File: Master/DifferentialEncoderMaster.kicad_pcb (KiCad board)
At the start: 2 copper layers, 53 x 131 mm, 41 parts, among them J1 RJ45_Shielded, J10 Conn_02x06_Top_Bottom, J11 Conn_02x06_Top_Bottom, J12 CAN_Header, J2 Conn_01x06, J3 Conn_01x20, J4 Conn_01x12, J5 RJ45_Shielded, J6 RJ45_Shielded, J7 RJ45_Shielded, J8 Jumper, J9 Jumper, U1 SN75C1167, U2 SN75C1167, U3 ST26C32ABTR, U4 ST26C32ABTR

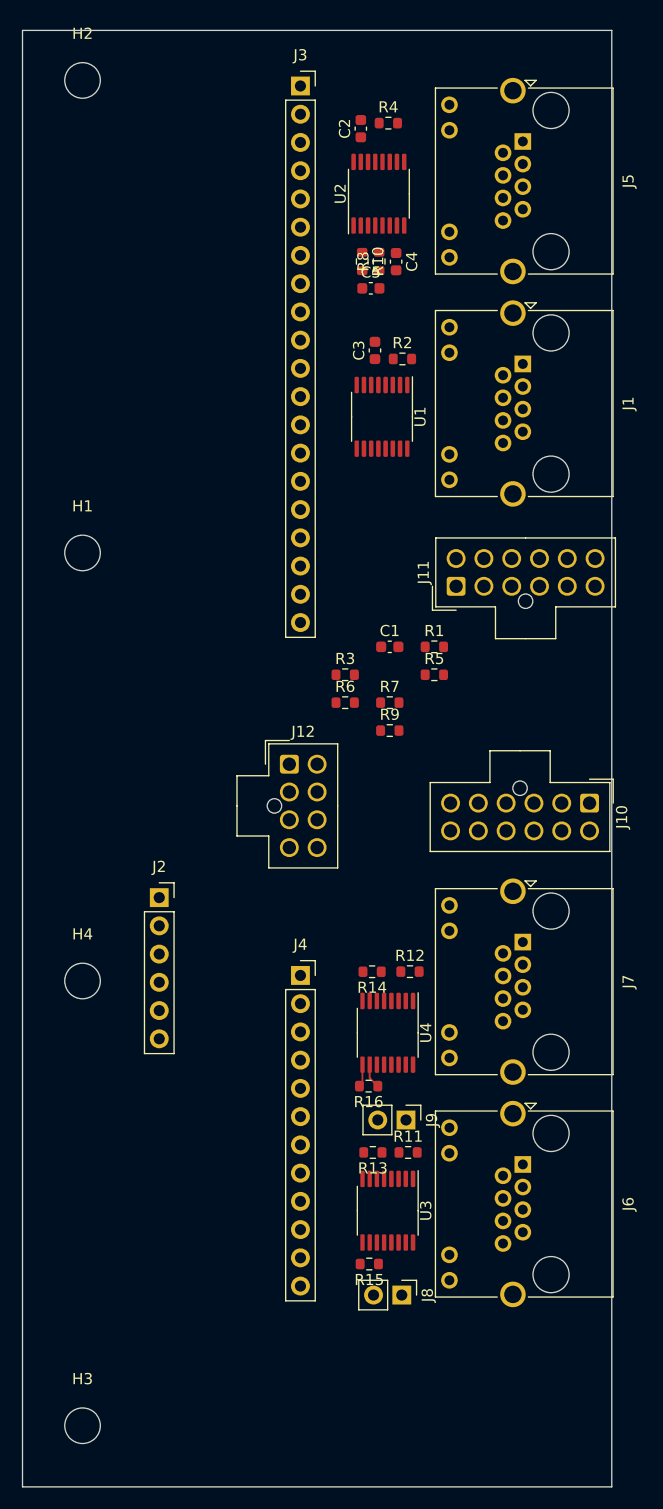
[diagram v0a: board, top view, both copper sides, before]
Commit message: Add digital isolators
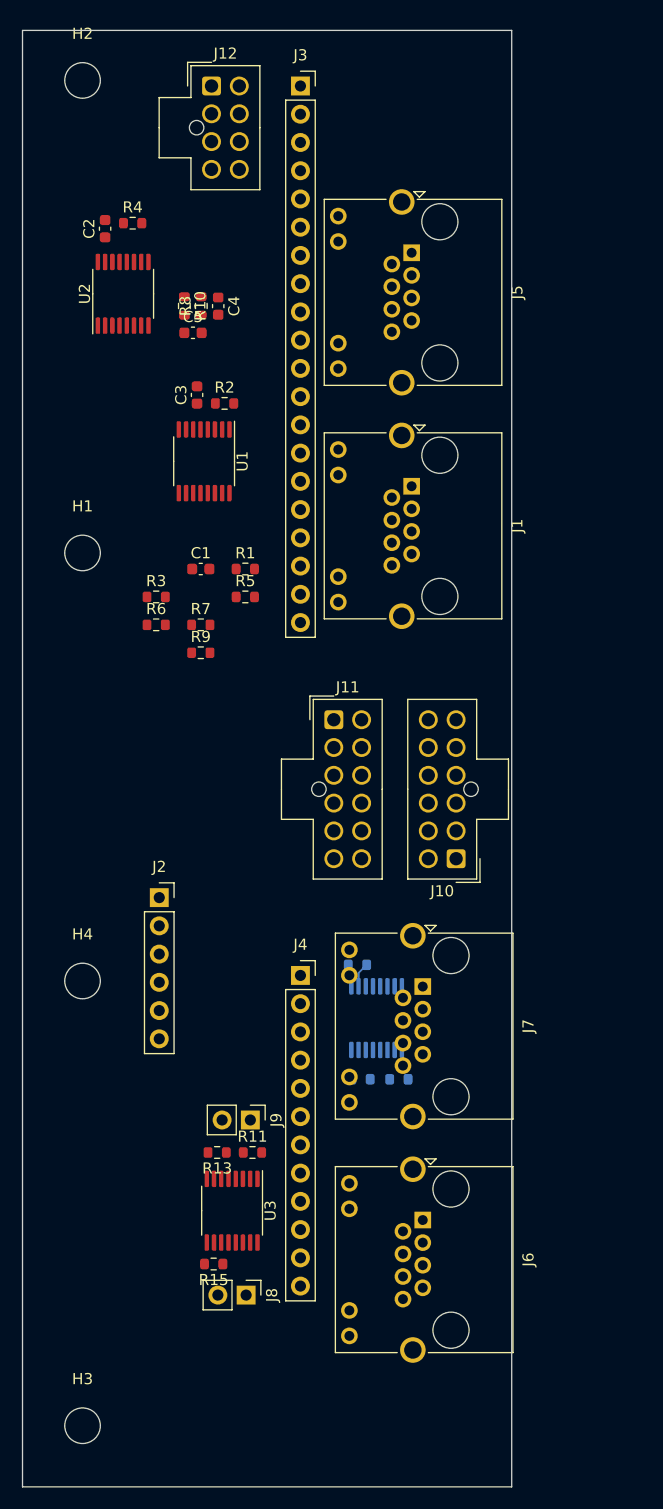
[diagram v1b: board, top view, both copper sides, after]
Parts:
- R12, R14, R16, U4: moved to B.Cu
- moved J12 61.4 mm to (117.0, 50.0)
- moved C2 24.7 mm to (107.4, 62.8)
- moved R4 24.7 mm to (109.9, 62.3)
- moved U2 24.7 mm to (109.1, 68.7)
- moved C1 18.4 mm to (116.0, 93.4)
- moved R7 18.4 mm to (116.0, 98.5)
- moved R9 18.4 mm to (116.0, 101.0)
- moved R1 18.4 mm to (120.0, 93.4)
- moved R3 18.4 mm to (112.0, 96.0)
- moved R5 18.4 mm to (120.0, 96.0)
- moved R6 18.4 mm to (112.0, 98.5)
- moved C3 16.5 mm to (115.7, 77.8)
- moved C4 16.5 mm to (117.6, 69.8)
- moved R10 16.5 mm to (114.6, 69.8)
- moved R2 16.5 mm to (118.2, 78.5)
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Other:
- board size 53 x 131 mm -> 44 x 131 mm

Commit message: Big updates to master
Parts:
- removed J6, J7: RJ45_Shielded, Connector_RJ:RJ45_Amphenol_RJHSE538X
- added C10: 100nF, Capacitor_SMD:C_0603_1608Metric, F.Cu at (142.6, 122.6)
- added C11: 100nF, Capacitor_SMD:C_0603_1608Metric, F.Cu at (142.0, 165.9)
- added C6: 100nF, Capacitor_SMD:C_0603_1608Metric, F.Cu at (136.9, 96.5)
- added C7: 100nF, Capacitor_SMD:C_0603_1608Metric, F.Cu at (116.5, 80.1)
- added C8: 100nF, Capacitor_SMD:C_0603_1608Metric, F.Cu at (129.3, 55.5)
- added C9: 100nF, Capacitor_SMD:C_0603_1608Metric, F.Cu at (114.8, 83.2)
- added FB1: 1kR, Inductor_SMD:L_0603_1608Metric, F.Cu at (114.8, 80.0)
- added FB2: 1kR, Inductor_SMD:L_0603_1608Metric, F.Cu at (116.5, 83.2)
- added J13: ISO_GPIO, Connector_Molex:Molex_Nano-Fit_105310-xx08_2x04_P2.50mm_Vertical, F.Cu at (107.2, 71.8)
- added R17: 3.3k, Resistor_SMD:R_0603_1608Metric, F.Cu at (142.0, 168.5)
- added R18: 3.3k, Resistor_SMD:R_0603_1608Metric, F.Cu at (142.6, 125.2)
- added R19: 0R, Resistor_SMD:R_0603_1608Metric, F.Cu at (135.3, 49.4)
- added R20: 0R, Resistor_SMD:R_0603_1608Metric, F.Cu at (134.9, 104.0)
- added U6: ISO7761DBQ, Package_SO:SSOP-16_3.9x4.9mm_P0.635mm, F.Cu at (111.0, 81.6)
- J1, J5: value RJ45_Shielded -> RJ45_Shielded_x2; footprint Connector_RJ:RJ45_Amphenol_RJHSE538X -> Wetmelon:RJ45_RJSSE5380-02
- J10: value Conn_02x06_Top_Bottom -> Encoder_0
- J11: value Conn_02x06_Top_Bottom -> Encoder_1
- R12, R14, R16, U4: moved to F.Cu
- moved J5 92.7 mm to (128.9, 157.5), turned to 90 degrees
- moved R5 50.9 mm to (142.8, 50.4), turned to 270 degrees
- moved J10 49.9 mm to (105.8, 156.8), turned to 90 degrees
- moved C1 49.8 mm to (141.2, 50.4), turned to 90 degrees
- moved R7 49.4 mm to (129.5, 50.9)
- moved C2 48.6 mm to (140.5, 98.4), turned to 0 degrees
- moved R3 46.5 mm to (129.5, 52.9)
- moved R8 42.0 mm to (140.5, 104.0), turned to 180 degrees
- moved J11 40.9 mm to (118.2, 146.8), turned to 270 degrees
- moved R4 40.9 mm to (129.7, 98.1), turned to 90 degrees
- moved U2 40.6 mm to (134.8, 100.0), turned to 0 degrees
- moved C4 39.7 mm to (140.5, 102.3), turned to 0 degrees
- moved U1 36.0 mm to (135.4, 53.2), turned to 180 degrees
- moved R16 35.5 mm to (137.2, 163.8), turned to 0 degrees
- moved U4 34.6 mm to (136.4, 168.1), turned to 0 degrees
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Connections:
- J1 pad 10: (no net) -> /CSn_2-
- J1 pad 11: (no net) -> /CLK_2+
- J1 pad 12: (no net) -> /MISO_2-
- J1 pad 9: (no net) -> /CSn_2+
- J10 pad 12: /AGND -> (no net)
- J10 pad 6: /GPIO5 -> (no net)
- J11 pad 12: /AGND -> (no net)
- J11 pad 6: /GPIO6 -> (no net)
- J2 pad 3: /SWC -> (no net)
- J2 pad 5: /SWD -> (no net)
- J2 pad 6: /~RST -> (no net)
- J3 pad 10: /MOSI -> (no net)
- J3 pad 6: /AVCC -> (no net)
- J3 pad 7: /AGND -> (no net)
- J5 pad 1: /CSn_2+ -> /ENC0_A+
- J5 pad 10: (no net) -> /ENC1_A-
- J5 pad 11: (no net) -> /ENC1_B+
- J5 pad 12: (no net) -> /ENC1_Z-
- J5 pad 2: /CSn_2- -> /ENC0_A-
- J5 pad 3: /CLK_2+ -> /ENC0_B+
- J5 pad 4: /MISO_2- -> /ENC0_Z-
- J5 pad 5: /MISO_2+ -> /ENC0_Z+
- J5 pad 6: /CLK_2- -> /ENC0_B-
- J5 pad 9: (no net) -> /ENC1_A+
- R7 pad 1: /GPIO7 -> /GPIO5
- R8 pad 1: /GPIO8 -> /GPIO6
- U1 pad 4: /CSn_1 -> Net-(R19-Pad2)
- U1 pad 5: Net-(U1-Pad5) -> (no net)
- U1 pad 6: Net-(U1-Pad6) -> (no net)
- U1 pad 7: Net-(U1-Pad7) -> (no net)
- U2 pad 4: /CSn_2 -> Net-(R20-Pad2)
- U2 pad 5: Net-(U2-Pad5) -> (no net)
- U2 pad 6: Net-(U2-Pad6) -> (no net)
- U2 pad 7: Net-(U2-Pad7) -> (no net)
- U3 pad 12: Net-(J8-Pad1) -> Net-(J9-Pad1)
- U3 pad 13: Net-(U3-Pad13) -> (no net)
- U3 pad 14: Net-(U3-Pad14) -> (no net)
- U3 pad 15: Net-(U3-Pad15) -> (no net)
- U3 pad 4: +5V -> GNDD
- U4 pad 12: Net-(J9-Pad1) -> Net-(J8-Pad1)
- U4 pad 13: Net-(U4-Pad13) -> (no net)
- U4 pad 14: Net-(U4-Pad14) -> (no net)
- U4 pad 15: Net-(U4-Pad15) -> (no net)
- U4 pad 4: +5V -> GNDD
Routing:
- net /CSn_2+: track 0.00 -> 32.5 mm, vias 0 -> 2
- net /CSn_2-: track 0.00 -> 30.7 mm, vias 0 -> 2
- net GNDD: track 0.00 -> 30.7 mm, vias 0 -> 10
- net /CLK_2-: track 0.00 -> 25.0 mm, vias 0 -> 2
- net /CLK_2+: track 0.00 -> 25.0 mm, vias 0 -> 2
- net +5V: track 0.00 -> 24.6 mm, vias 0 -> 7
- net /M1_Z: track 0.00 -> 23.5 mm
- net VDD1: track 0.00 -> 23.5 mm, vias 0 -> 1
- net /MISO_2-: track 0.00 -> 23.5 mm, vias 0 -> 2
- net /M1_B: track 0.00 -> 22.6 mm
- net /GPIO1: track 0.00 -> 22.1 mm
- net /MISO_2+: track 0.00 -> 22.1 mm, vias 0 -> 2
- net /M1_A: track 0.00 -> 21.4 mm
- net /M0_Z: track 0.00 -> 20.6 mm
- net /M0_A: track 0.00 -> 20.4 mm
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- added copper zone on In2.Cu, net +5V
- added copper zone on In1.Cu, net GNDD
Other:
- board size 44 x 131 mm -> 46.5 x 131 mm
- copper layers 2 -> 4
- net class Default: clearance 0.1651 -> 0.2032; trace_width 0.1651 -> 0.2032
- rule trace_clearance: 0.1651 -> 0.2032

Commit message: Finish rev 1 layout
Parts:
- moved J8 54.3 mm to (135.5, 118.9), turned to 90 degrees
- moved J9 51.0 mm to (136.0, 170.7), turned to 90 degrees
- moved C10 46.8 mm to (131.6, 168.1), turned to 180 degrees
- moved R14 46.2 mm to (141.9, 122.8), turned to 90 degrees
- moved R11 45.8 mm to (142.4, 167.6), turned to 270 degrees
- moved R17 45.0 mm to (131.4, 124.7), turned to 180 degrees
- moved U4 44.1 mm to (137.0, 124.1), turned to 180 degrees
- moved R18 42.7 mm to (131.6, 166.5), turned to 180 degrees
- moved R16 41.8 mm to (132.1, 122.3), turned to 90 degrees
- moved U3 40.9 mm to (137.2, 165.8), turned to 180 degrees
- moved C11 40.9 mm to (131.4, 126.4), turned to 180 degrees
- moved R13 39.7 mm to (142.4, 164.5), turned to 90 degrees
- moved R12 38.7 mm to (141.9, 126.0), turned to 270 degrees
- moved R15 37.8 mm to (132.1, 163.8)
- moved C3 14.9 mm to (141.7, 57.8), turned to 0 degrees
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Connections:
- J13 pad 1: VDD1 -> /ISO_STEP_2
- J13 pad 2: GND1 -> /ISO_DIR_2
- J13 pad 3: /ISO_DIR_1 -> /ISO_UART_RX
- J13 pad 4: /ISO_STEP_1 -> /ISO_UART_TX
- J13 pad 5: /ISO_UART_TX -> /ISO_STEP_1
- J13 pad 6: /ISO_UART_RX -> /ISO_DIR_1
- J13 pad 7: /ISO_DIR_2 -> GND1
- J13 pad 8: /ISO_STEP_2 -> VDD1
- J2 pad 2: /+3.3V -> (no net)
- J3 pad 1: /+3.3V -> (no net)
- J4 pad 1: /+3.3V -> (no net)
- J4 pad 7: /+3.3V -> (no net)
- J5 pad 1: /ENC0_A+ -> /ENC1_A+
- J5 pad 10: /ENC1_A- -> /ENC0_A-
- J5 pad 11: /ENC1_B+ -> /ENC0_B+
- J5 pad 12: /ENC1_Z- -> /ENC0_Z-
- J5 pad 13: /ENC1_Z+ -> /ENC0_Z+
- J5 pad 14: /ENC1_B- -> /ENC0_B-
- J5 pad 2: /ENC0_A- -> /ENC1_A-
- J5 pad 3: /ENC0_B+ -> /ENC1_B+
- J5 pad 4: /ENC0_Z- -> /ENC1_Z-
- J5 pad 5: /ENC0_Z+ -> /ENC1_Z+
- J5 pad 6: /ENC0_B- -> /ENC1_B-
- J5 pad 9: /ENC1_A+ -> /ENC0_A+
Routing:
- net /SCK: track 0.00 -> 72.7 mm, vias 0 -> 6
- net /MISO_2: track 0.00 -> 44.5 mm, vias 0 -> 2
- net /ENC0_A+: track 0.00 -> 43.2 mm, vias 0 -> 2
- net /GPIO5: track 0.00 -> 42.8 mm, vias 0 -> 3
- net /ENC0_A-: track 0.00 -> 41.2 mm, vias 0 -> 2
- net /ENC1_B-: track 0.00 -> 35.3 mm
- net /ENC1_B+: track 0.00 -> 33.8 mm
- net /M0_A: track 20.4 -> 53.1 mm, vias 0 -> 1
- net /ENC0_B+: track 0.00 -> 32.4 mm, vias 0 -> 1
- net /M1_B: track 22.6 -> 54.3 mm, vias 0 -> 3
- net /GPIO6: track 0.00 -> 31.2 mm, vias 0 -> 1
- net /ENC1_A-: track 0.00 -> 31.1 mm, vias 0 -> 2
- net /ENC0_B-: track 0.00 -> 31.0 mm, vias 0 -> 1
- net /M0_Z: track 20.6 -> 51.4 mm, vias 0 -> 1
- net /ENC1_A+: track 0.00 -> 30.6 mm, vias 0 -> 2
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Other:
- board text added: "+5V"
- board text added: "CAN"
- board text added: "CANH"
- board text added: "CANL"
- board text added: "DIR1"
- board text added: "DIR2"
- board text added: "GND"
- board text added: "GND1"
- board text added: "GND1 / VDD1 Isolated"
- board text added: "GPIO"
- board text added: "STEP1"
- board text added: "STEP2"
- board text added: "U_RX"
- board text added: "U_TX"
- board text added: "VDD1"

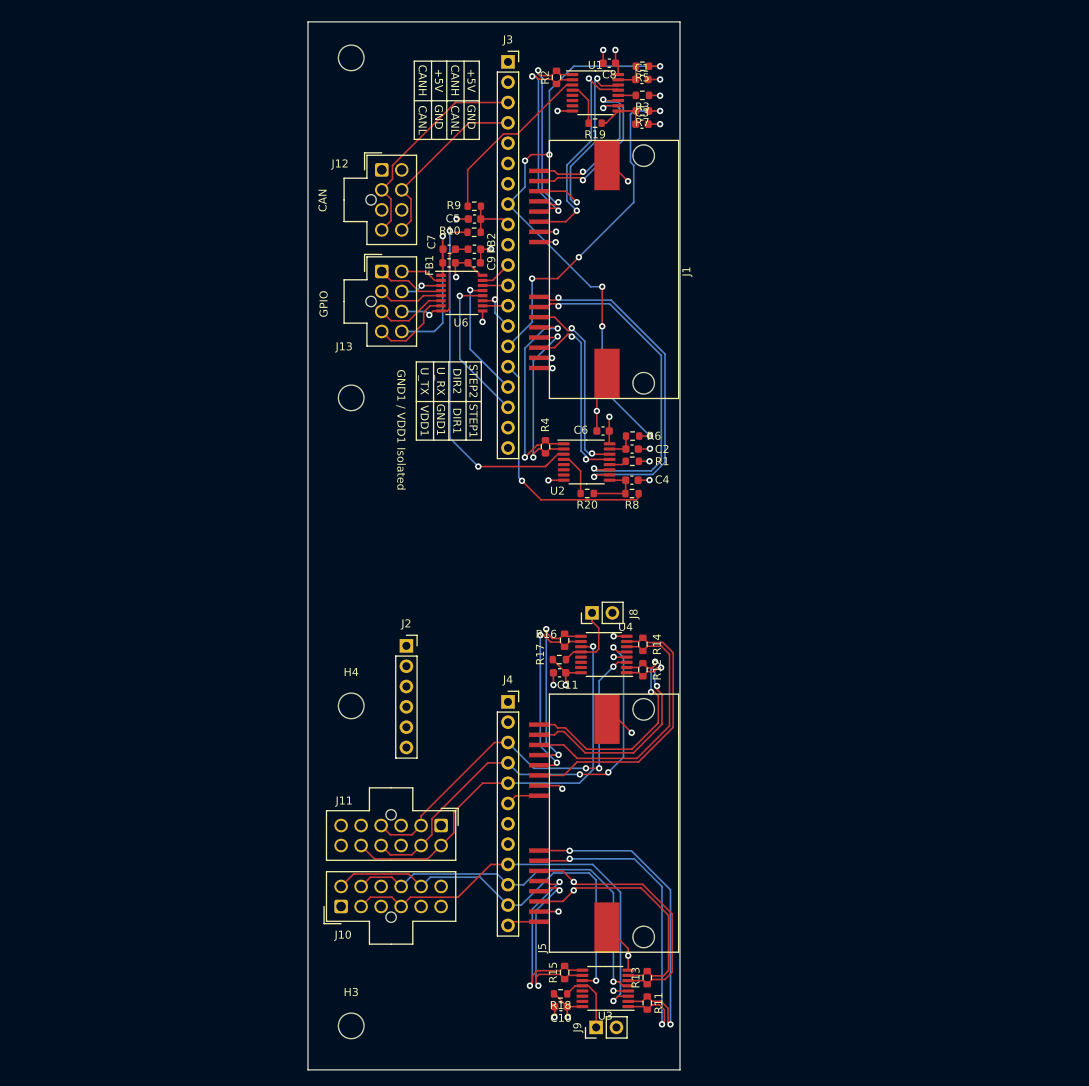
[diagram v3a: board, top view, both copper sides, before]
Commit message: Rotate board and recreate planes
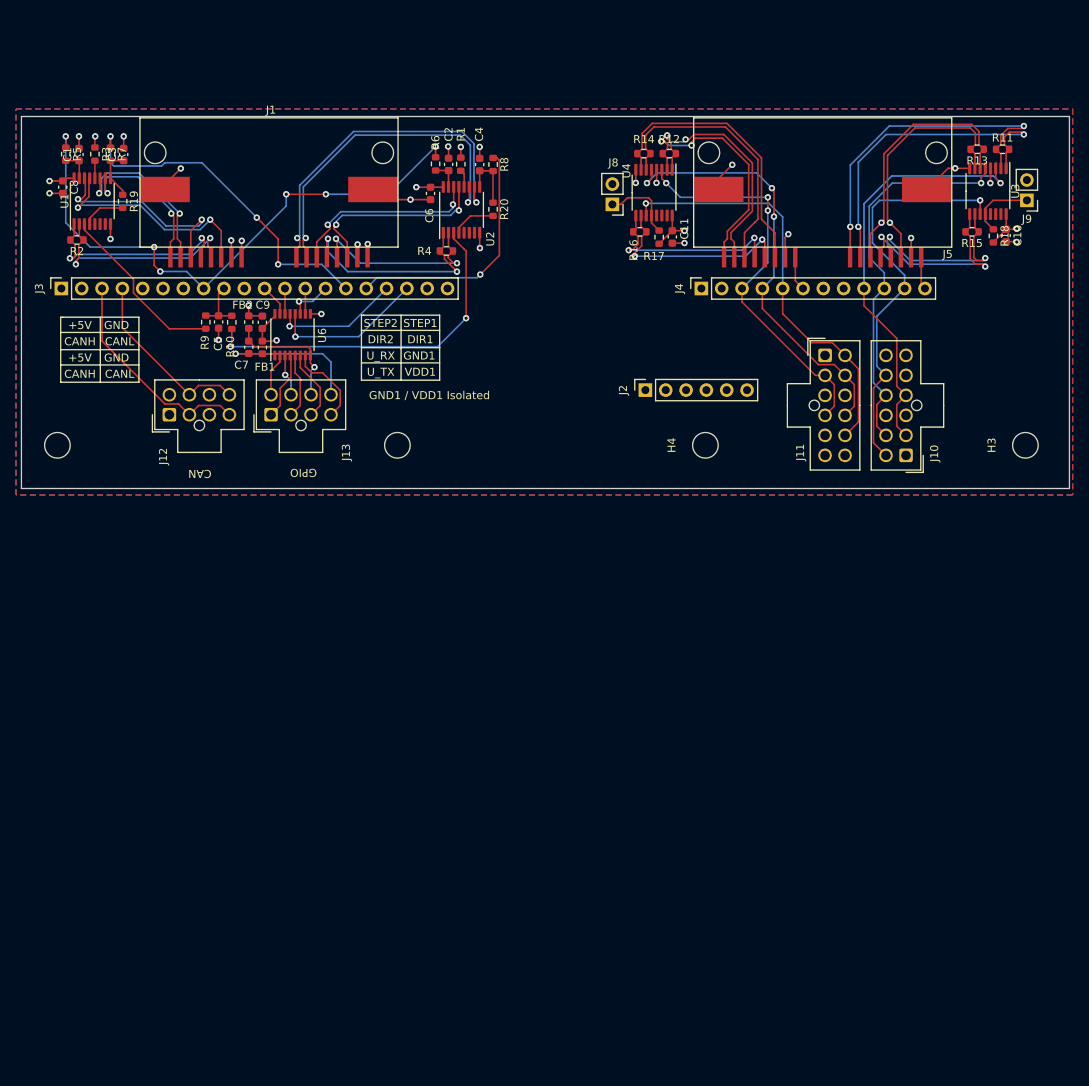
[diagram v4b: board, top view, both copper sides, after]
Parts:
- moved J9 116.6 mm to (189.9, 67.3), turned to 180 degrees
- moved R11 115.6 mm to (186.8, 60.9), turned to 0 degrees
- moved R13 111.5 mm to (183.7, 60.9), turned to 180 degrees
- moved C10 111.3 mm to (187.3, 71.7), turned to 270 degrees
- moved H3 111.2 mm to (189.7, 97.9), turned to 90 degrees
- moved U3 110.5 mm to (185.0, 66.2), turned to 270 degrees
- moved R18 109.1 mm to (185.7, 71.8), turned to 270 degrees
- moved R15 105.7 mm to (183.0, 71.2), turned to 180 degrees
- moved J5 95.8 mm to (176.7, 74.4), turned to 180 degrees
- moved J10 90.4 mm to (174.8, 99.2), turned to 180 degrees
- moved J11 75.9 mm to (164.6, 86.7), turned to 0 degrees
- moved R5 72.9 mm to (69.7, 61.5), turned to 270 degrees
- moved C1 71.0 mm to (71.4, 61.6), turned to 90 degrees
- moved C8 70.1 mm to (69.3, 65.7), turned to 270 degrees
- moved R3 68.8 mm to (73.4, 61.5), turned to 270 degrees
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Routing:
- added copper zone on B.Cu, net GNDD
- added copper zone on F.Cu, net GNDD
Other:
- board size 46.5 x 131 mm -> 131 x 46.5 mm

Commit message: Minor changes to silkscreen etc
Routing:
- net GNDD: track 60.7 -> 56.6 mm, vias 21 -> 20
- net /CSn_1+: track 20.1 -> 16.8 mm
- net /CSn_1-: track 21.8 -> 19.5 mm

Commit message: Update Master
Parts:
- J2: moved to B.Cu
- moved J10 11.6 mm to (178.0, 88.0), turned to 90 degrees
- moved J11 4.81 mm to (160.0, 88.0), turned to 90 degrees
- moved J13 0.63 mm to (96.0, 94.0)
- moved J12 0.34 mm to (83.0, 94.0)
- turned J2 to 270 degrees
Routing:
- net /M1_Z: track 52.8 -> 47.0 mm
- net /M0_Z: track 51.4 -> 47.2 mm
- net /M1_B: track 54.3 -> 51.0 mm
- net /M0_A: track 53.1 -> 55.3 mm
- net /M1_A: track 49.9 -> 52.0 mm
- net /ISO_UART_TX: track 10.5 -> 11.5 mm
- net /CAN_H: track 27.3 -> 26.3 mm
- net /ISO_UART_RX: track 8.92 -> 9.57 mm
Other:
- board text added: "3.3V"
- board text added: "5V"
- board text added: "A"
- board text added: "B"
- board text added: "M0"
- board text added: "M1"
- board text added: "NC"
- board text added: "Pinout"
- board text added: "U"
- board text added: "V"
- board text added: "W"
- board text added: "Z"
